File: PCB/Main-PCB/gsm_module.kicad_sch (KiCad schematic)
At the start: 6 parts, among them J1 SIM_Card, U1 SIM800C

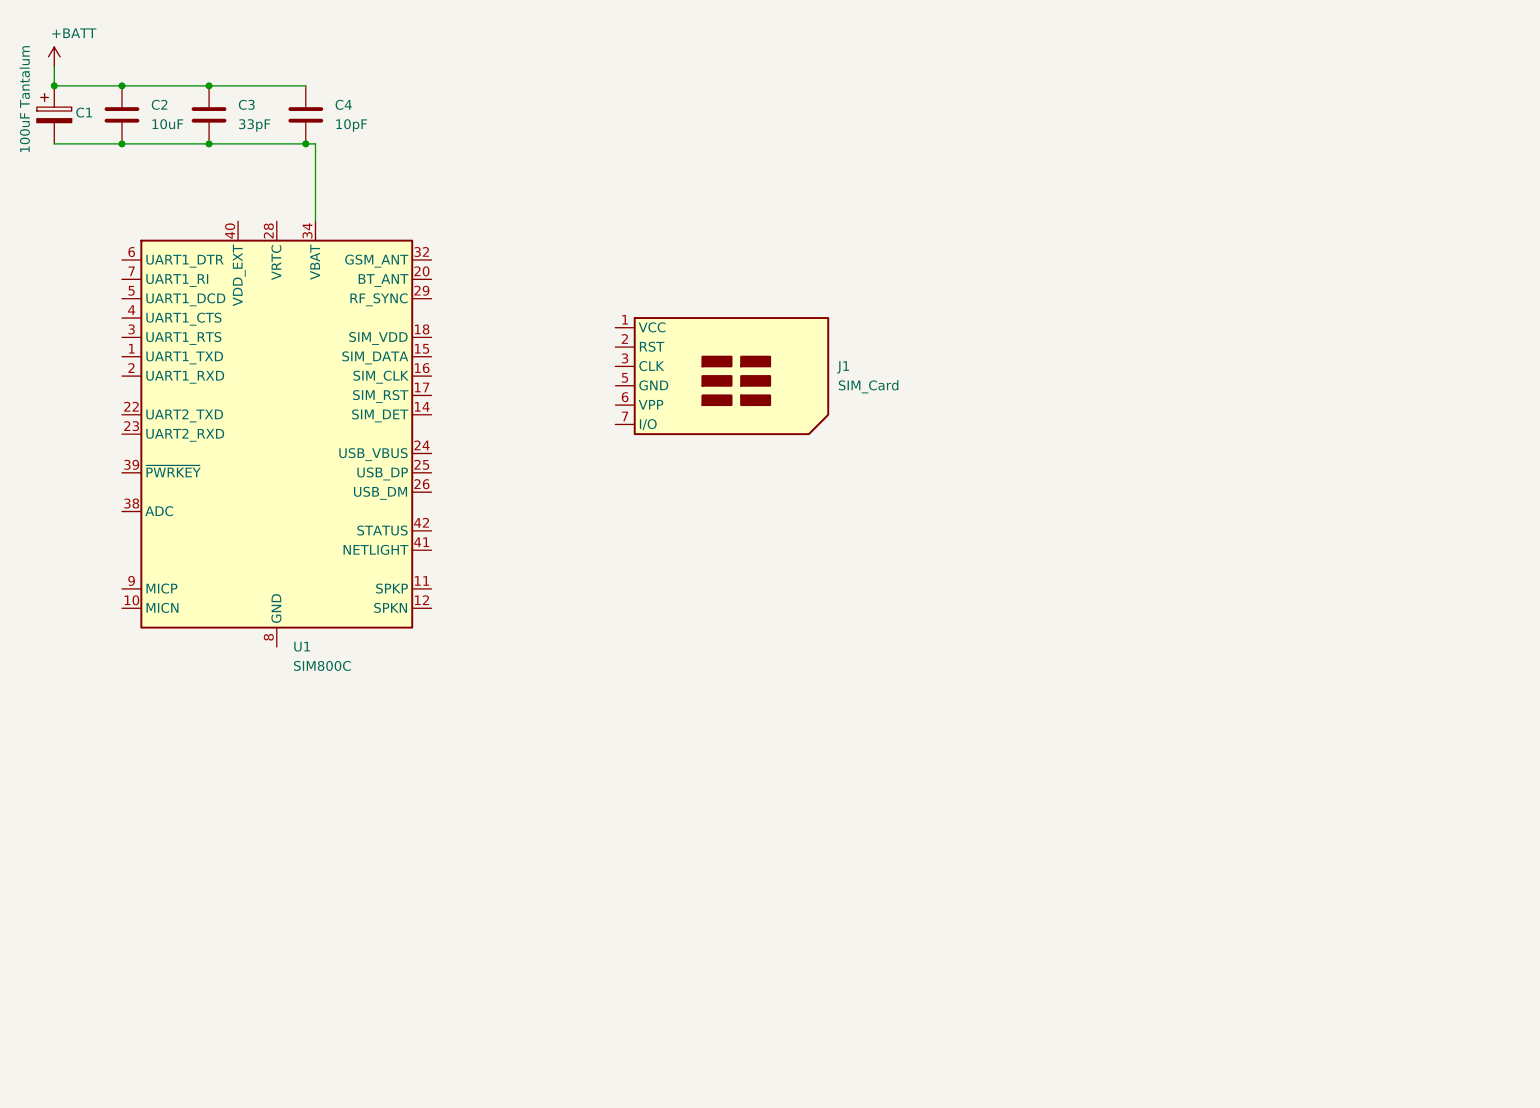
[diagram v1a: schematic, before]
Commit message: Finished schematic for SIM800C and power chips
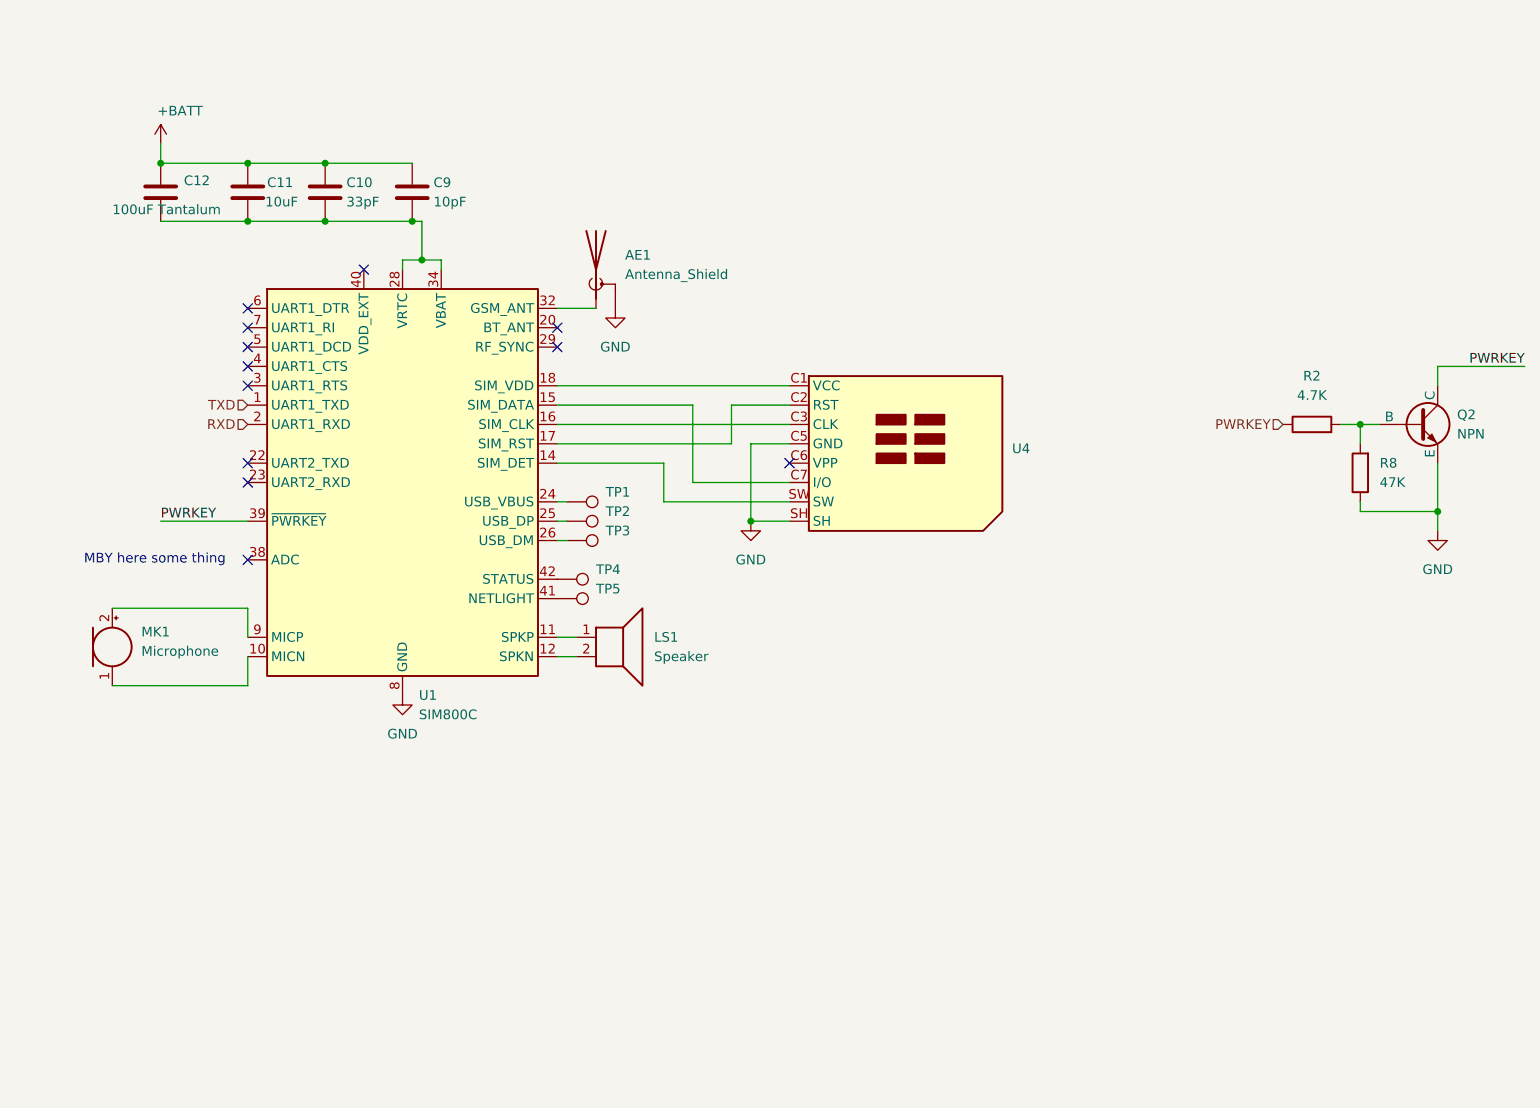
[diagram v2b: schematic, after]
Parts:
- removed C1: 100uF Tantalum, symbol Device:C_Polarized
- removed C2: 10uF, symbol Device:C
- removed C3: 33pF, symbol Device:C
- removed C4: 10pF, symbol Device:C
- removed J1: SIM_Card, symbol Connector:SIM_Card
- added AE1: Antenna_Shield, symbol Device:Antenna_Shield
- added C10: 33pF, symbol Device:C
- added C11: 10uF, symbol Device:C
- added C12: 100uF Tantalum, symbol Device:C
- added C9: 10pF, symbol Device:C
- added LS1: Speaker, symbol Device:Speaker
- added MK1: Microphone, symbol Device:Microphone
- added Q2: NPN, symbol Simulation_SPICE:NPN
- added R2: 4.7K, symbol Device:R
- added R8: 47K, symbol Device:R
- added TP1, TP2, TP3, TP4, TP5: TestPoint, symbol Connector:TestPoint
- added U4: ~, symbol Components:SIM
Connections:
- net +BATT: now also C10.1, C11.1, C12.1, C9.1
- net at U1.34 (VBAT), U1.35 (VBAT): now also U1.28 (VRTC), C10.2, C11.2, C12.2, C9.2
- net TXD: now reaches U1.1 (UART1_TXD)
- net at U1.10 (MICN): now also MK1.1 (-)
- net at U1.11 (SPKP): now also LS1.1
- net at U1.12 (SPKN): now also LS1.2
- net GND: now reaches U1.13 (GND), U1.19 (GND), U1.21 (GND), U1.27 (GND), U1.30 (GND), U1.31 (GND), U1.33 (GND), U1.36 (GND), U1.37 (GND), U1.8 (GND)
- net GND: now also AE1.2 (Shield), Q2.3 (E), R8.1, U4.C5 (GND), U4.SH
- net at U1.14 (SIM_DET): now also U4.SW
- net at U1.15 (SIM_DATA): now also U4.C7 (I/O)
- net at U1.16 (SIM_CLK): now also U4.C3 (CLK)
- net at U1.17 (SIM_RST): now also U4.C2 (RST)
- net at U1.18 (SIM_VDD): now also U4.C1 (VCC)
- net RXD: now reaches U1.2 (UART1_RXD)
- net at U1.24 (USB_VBUS): now also TP1.1
- net at U1.25 (USB_DP): now also TP2.1
- net at U1.26 (USB_DM): now also TP3.1
- net at U1.32 (GSM_ANT): now also AE1.1 (A)
- net PWRKEY: now reaches U1.39 (~{PWRKEY})
- net PWRKEY: now also Q2.1 (C), R2.1
- net at U1.41 (NETLIGHT): now also TP5.1
- net at U1.42 (STATUS): now also TP4.1
- net at U1.9 (MICP): now also MK1.2 (+)
- new net: Q2.2 (B), R2.2, R8.2
- no-connect marks 0 -> 12
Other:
- note added: "MBY here some thing"
- moved on the sheet: U1

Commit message: Added MCU scheme
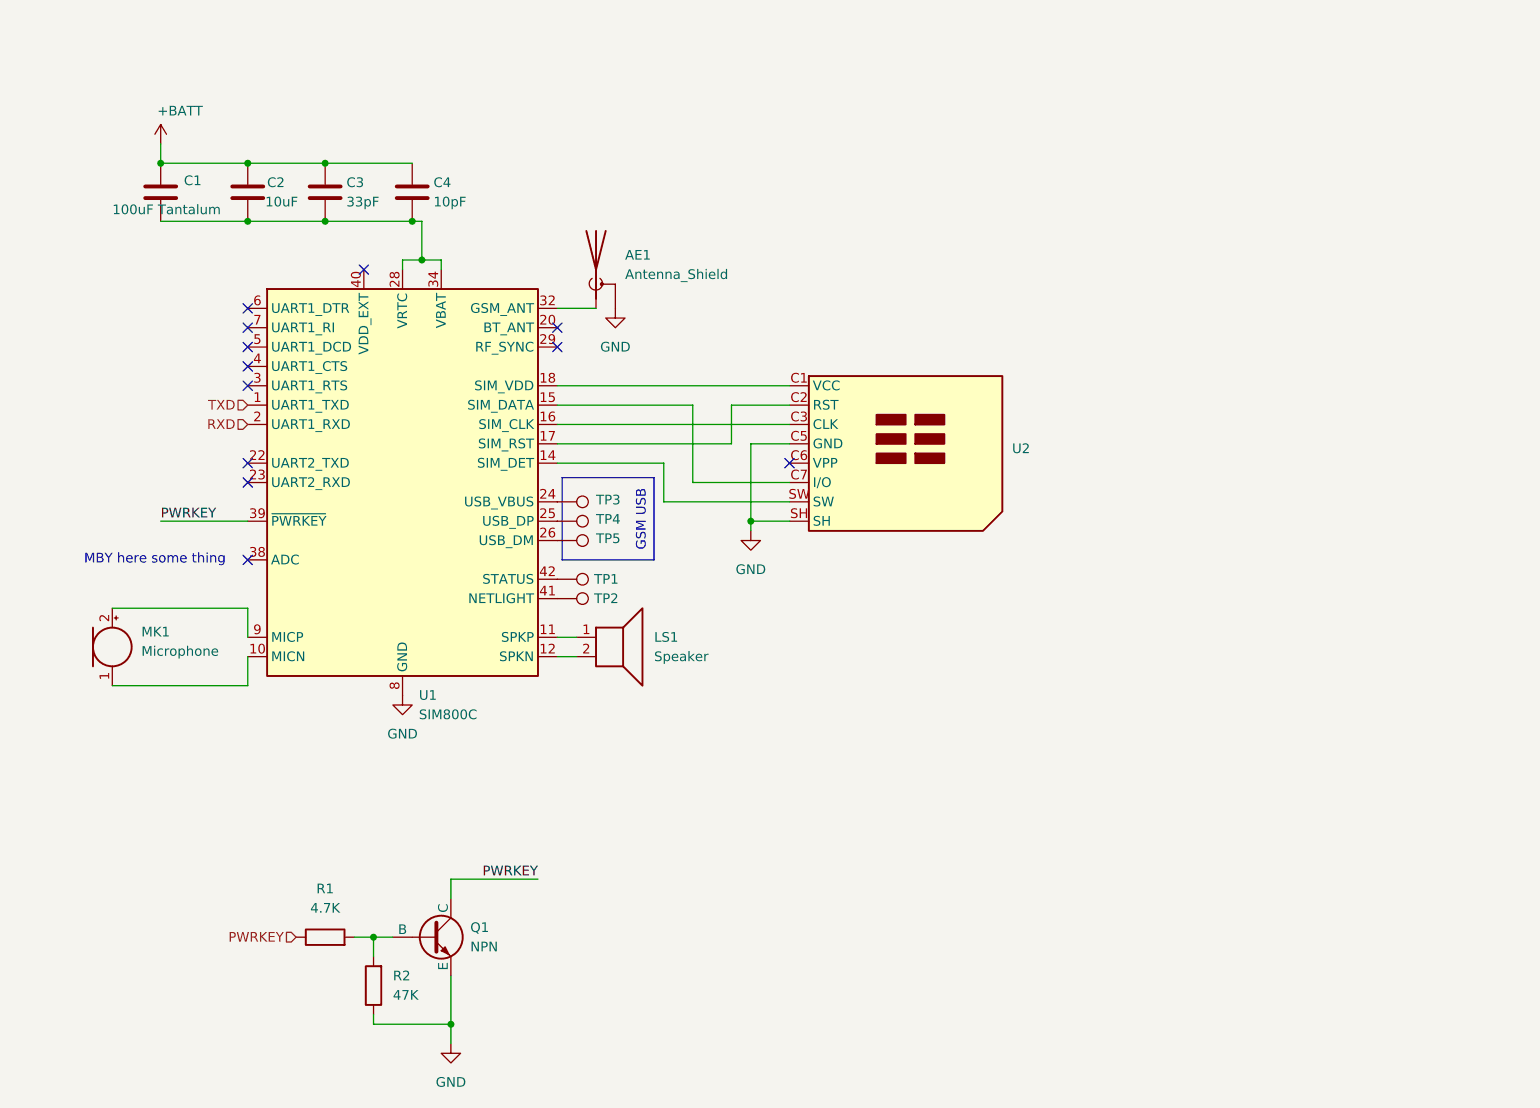
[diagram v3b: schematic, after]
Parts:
- renumbered C12 to C1, C11 to C2, C10 to C3, C9 to C4, Q2 to Q1, R2 to R1, R8 to R2, TP4 to TP1, TP5 to TP2, TP1 to TP3, TP2 to TP4, TP3 to TP5, U4 to U2
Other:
- moved on the sheet: Q1, R1, R2, TP3, TP4, TP5
